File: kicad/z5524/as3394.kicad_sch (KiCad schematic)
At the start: 35 parts, among them U11 DG442xY, U14 TL074, U15 AS3394

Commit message: dist ref cap to two 1u instead of single; some more silkscreen cleanup
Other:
- moved on the sheet: C44, C45, C46, C50, C53, C55, C60, C62, C64, C66, D3, D4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

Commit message: v0.3 Release
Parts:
- U11: value DG442xY -> DG442DY-T1-E3; LCSC C144269 -> C2673321
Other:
- note added: "Saw: +/-2.84V"
- note added: "TODO: use a 68k Basic part and re-eval VCO Output levels: expected levels differ from observed levels at 63x gain Waveshape Expected Observed Saw +/- 2.84V +/- 1.64V Tri +/- 3.15V -1.8 : +1.32V Saw+Tri -5.67 +2.84 -2.8 : +1.76V Pulse +/- 1.9V"
- note removed: "Saw: +/-2.8V TODO: measure observed"
- note removed: "VCO Output levels: expected levels differ from observed levels at 63x gain Waveshape Expected Observed Saw +/- 2.84V +/- 1.64V Tri +/- 3.15V -1.8 : +1.32V Saw+Tri -5.67 +2.84 -2.8 : +1.76V Pulse +/- 1.9V"
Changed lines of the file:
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@@
   (title_block
     (title "Zoxnoxious Z5524 (SSI2130/AS3394)")
-    (date "2023-12-06")
+    (date "2023-12-12")
     (rev "0.3")
     (company "Zoxnoxious Engineering")
@@
     (effects (font (size 1.27 1.27)) (justify left bottom))
   )
-  (text "Saw: +/-2.8V\nTODO: measure observed" (at 231.775 113.03 0)
+  (text "Saw: +/-2.84V" (at 231.775 113.03 0)
     (effects (font (size 1.27 1.27)) (justify left bottom))
   )
-  (text "VCO Output levels: expected levels\ndiffer from observed levels at 63x gain\nWaveshape	Expected			Observed\nSaw			+/- 2.84V		+/- 1.64V\nTri			+/- 3.15V		-1.8 : +1.32V\nSaw+Tri		-5.67 +2.84		-2.8 : +1.76V\nPulse		+/- 1.9V			"
+  (text "TODO: use a 68k Basic part and re-eval\nVCO Output levels: expected levels\ndiffer from observed levels at 63x gain\nWaveshape	Expected			Observed\nSaw			+/- 2.84V		+/- 1.64V\nTri			+/- 3.15V		-1.8 : +1.32V\nSaw+Tri		-5.67 +2.84		-2.8 : +1.76V\nPulse		+/- 1.9V			"
     (at 201.295 94.615 0)
     (effects (font (size 1.27 1.27)) (justify left bottom))
@@
       (effects (font (size 1.27 1.27)))
     )
-    (property "Value" "DG442xY" (at 331.47 67.4171 0)
+    (property "Value" "DG442DY-T1-E3" (at 331.47 67.4171 0)
       (effects (font (size 1.27 1.27)))
     )
@@
       (effects (font (size 1.27 1.27)) hide)
     )
-    (property "LCSC" "C144269" (at 331.47 71.12 0)
-      (effects (font (size 1.27 1.27)) hide)
-    )
+    (property "LCSC" "C2673321" (at 331.47 71.12 0)
+      (effects (font (size 1.27 1.27)) hide)
+    )

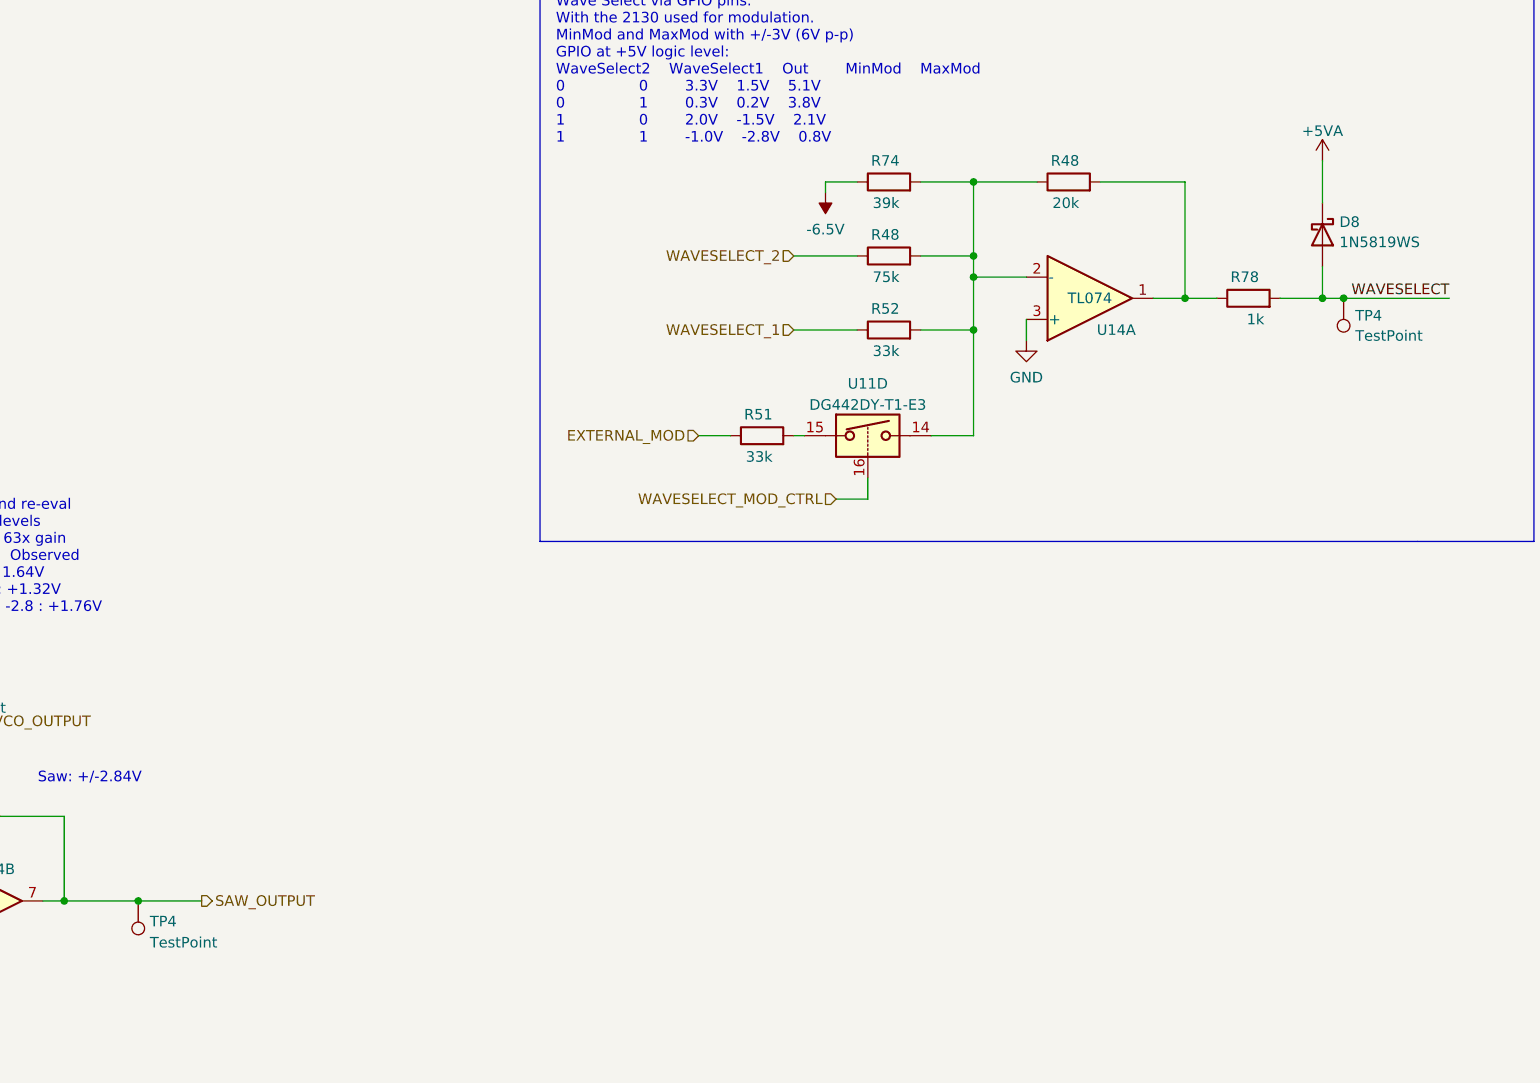
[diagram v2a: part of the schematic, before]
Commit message: updated routing and prep for z5524 revision rev.  Power routing going from polygons to direct
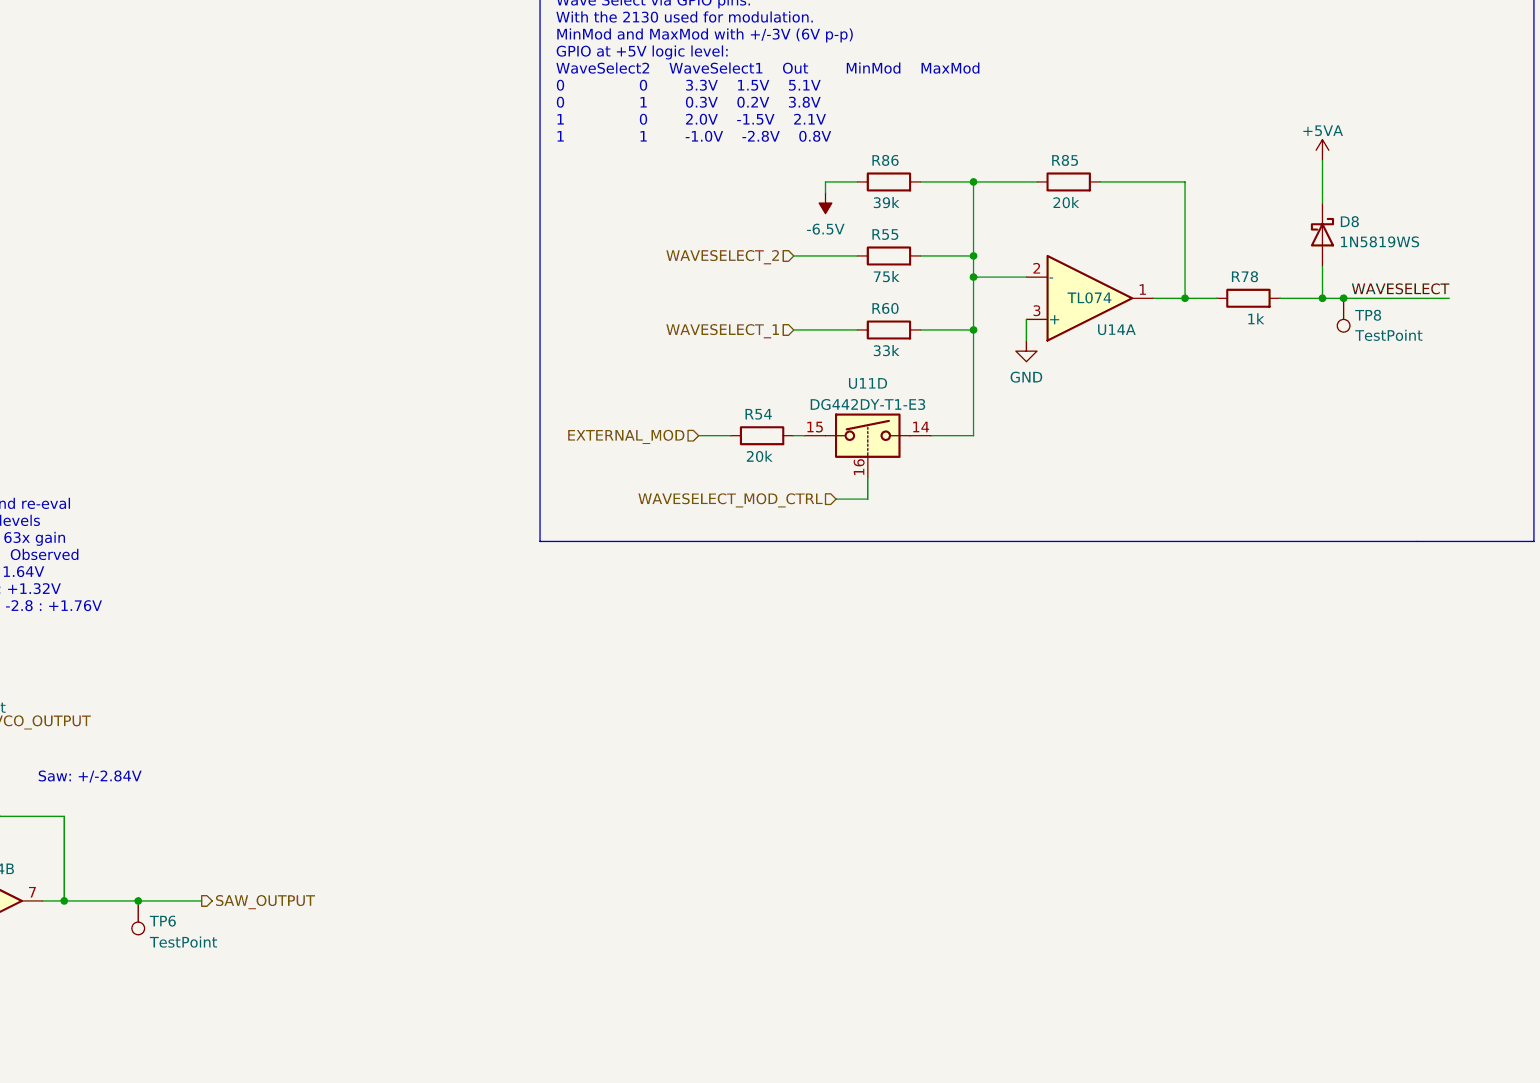
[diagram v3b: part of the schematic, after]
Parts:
- R54: renamed from R51; value 33k -> 20k; LCSC C4216 -> (none)
- renumbered R48 to R55, R52 to R60, R48 to R85, R74 to R86, TP4 to TP6, TP4 to TP8
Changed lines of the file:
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@@
   (symbol (lib_id "Device:R") (at 355.6 40.64 90) (unit 1)
     (in_bom yes) (on_board yes) (dnp no)
-    (property "Reference" "R48" (at 356.87 38.1 90)
+    (property "Reference" "R85" (at 356.87 38.1 90)
       (effects (font (size 1.27 1.27)) (justify left))
     )
@@
     (instances
       (project "z5524"
-        (path "/7079bdb0-a00e-4bac-b257-cbcf2c91bbd6"
-          (reference "R48") (unit 1)
-        )
         (path "/7079bdb0-a00e-4bac-b257-cbcf2c91bbd6/998834c5-8208-4d7e-a084-854ca45521ff"
           (reference "R85") (unit 1)
@@
   (symbol (lib_id "Device:R") (at 334.01 49.53 90) (unit 1)
     (in_bom yes) (on_board yes) (dnp no)
-    (property "Reference" "R48" (at 335.28 46.99 90)
+    (property "Reference" "R55" (at 335.28 46.99 90)
       (effects (font (size 1.27 1.27)) (justify left))
     )
@@
     (instances
       (project "z5524"
-        (path "/7079bdb0-a00e-4bac-b257-cbcf2c91bbd6"
-          (reference "R48") (unit 1)
-        )
         (path "/7079bdb0-a00e-4bac-b257-cbcf2c91bbd6/998834c5-8208-4d7e-a084-854ca45521ff"
           (reference "R55") (unit 1)
@@
   (symbol (lib_id "Device:R") (at 334.01 40.64 90) (unit 1)
     (in_bom yes) (on_board yes) (dnp no)
-    (property "Reference" "R74" (at 335.28 38.1 90)
+    (property "Reference" "R86" (at 335.28 38.1 90)
       (effects (font (size 1.27 1.27)) (justify left))
     )
@@
     (instances
       (project "z5524"
-        (path "/7079bdb0-a00e-4bac-b257-cbcf2c91bbd6"
+        (path "/7079bdb0-a00e-4bac-b257-cbcf2c91bbd6/998834c5-8208-4d7e-a084-854ca45521ff"
+          (reference "R86") (unit 1)
+        )
+      )
+    )
+  )
+  (symbol (lib_id "Device:R") (at 208.28 124.46 90) (unit 1)
+    (in_bom yes) (on_board yes) (dnp no)
+    (property "Reference" "R80" (at 209.55 121.92 90)
+      (effects (font (size 1.27 1.27)) (justify left))
+    )
+    (property "Value" "1k" (at 210.185 127 90)
+      (effects (font (size 1.27 1.27)) (justify left))
+    )
+    (property "Footprint" "Resistor_SMD:R_0603_1608Metric" (at 208.28 126.238 90)
+      (effects (font (size 1.27 1.27)) hide)
+    )
+    (property "Datasheet" "~" (at 208.28 124.46 0)
+      (effects (font (size 1.27 1.27)) hide)
+    )
+    (property "LCSC" "C21190" (at 208.28 124.46 0)
+      (effects (font (size 1.27 1.27)) hide)
+    )
+    (pin "1")
+    (pin "2")
+    (instances
+      (project "z5524"
+        (path "/7079bdb0-a00e-4bac-b257-cbcf2c91bbd6/998834c5-8208-4d7e-a084-854ca45521ff"
+          (reference "R80") (unit 1)
+        )
+      )
+    )
+  )
+  (symbol (lib_id "Device:R") (at 59.69 34.29 90) (unit 1)
+    (in_bom yes) (on_board yes) (dnp no)
+    (property "Reference" "R74" (at 58.42 39.37 0)
+      (effects (font (size 1.27 1.27)) (justify left))
+    )
+    (property "Value" "75k" (at 60.96 40.64 0)
+      (effects (font (size 1.27 1.27)) (justify left))
+    )
+    (property "Footprint" "Resistor_SMD:R_0603_1608Metric" (at 59.69 36.068 90)
+      (effects (font (size 1.27 1.27)) hide)
+    )
+    (property "Datasheet" "~" (at 59.69 34.29 0)
+      (effects (font (size 1.27 1.27)) hide)
+    )
+    (property "LCSC" "C23242" (at 59.69 34.29 0)
+      (effects (font (size 1.27 1.27)) hide)
+    )
+    (pin "1")
+    (pin "2")
+    (instances
+      (project "z5524"
+        (path "/7079bdb0-a00e-4bac-b257-cbcf2c91bbd6/998834c5-8208-4d7e-a084-854ca45521ff"
           (reference "R74") (unit 1)
         )
-        (path "/7079bdb0-a00e-4bac-b257-cbcf2c91bbd6/998834c5-8208-4d7e-a084-854ca45521ff"
-          (reference "R86") (unit 1)
-        )
-      )
-    )
-  )
-  (symbol (lib_id "Device:R") (at 208.28 124.46 90) (unit 1)
-    (in_bom yes) (on_board yes) (dnp no)
-    (property "Reference" "R80" (at 209.55 121.92 90)
-      (effects (font (size 1.27 1.27)) (justify left))
-    )
-    (property "Value" "1k" (at 210.185 127 90)
-      (effects (font (size 1.27 1.27)) (justify left))
-    )
-    (property "Footprint" "Resistor_SMD:R_0603_1608Metric" (at 208.28 126.238 90)
-      (effects (font (size 1.27 1.27)) hide)
-    )
-    (property "Datasheet" "~" (at 208.28 124.46 0)
-      (effects (font (size 1.27 1.27)) hide)
-    )
-    (property "LCSC" "C21190" (at 208.28 124.46 0)
-      (effects (font (size 1.27 1.27)) hide)
-    )
-    (pin "1")
-    (pin "2")
-    (instances
-      (project "z5524"
-        (path "/7079bdb0-a00e-4bac-b257-cbcf2c91bbd6/998834c5-8208-4d7e-a084-854ca45521ff"
-          (reference "R80") (unit 1)
-        )
-      )
-    )
-  )
-  (symbol (lib_id "Device:R") (at 59.69 34.29 90) (unit 1)
-    (in_bom yes) (on_board yes) (dnp no)
-    (property "Reference" "R74" (at 58.42 39.37 0)
-      (effects (font (size 1.27 1.27)) (justify left))
-    )
-    (property "Value" "75k" (at 60.96 40.64 0)
-      (effects (font (size 1.27 1.27)) (justify left))
-    )
-    (property "Footprint" "Resistor_SMD:R_0603_1608Metric" (at 59.69 36.068 90)
-      (effects (font (size 1.27 1.27)) hide)
-    )
-    (property "Datasheet" "~" (at 59.69 34.29 0)
-      (effects (font (size 1.27 1.27)) hide)
-    )
-    (property "LCSC" "C23242" (at 59.69 34.29 0)
-      (effects (font (size 1.27 1.27)) hide)
-    )
-    (pin "1")
-    (pin "2")
-    (instances
-      (project "z5524"
-        (path "/7079bdb0-a00e-4bac-b257-cbcf2c91bbd6/998834c5-8208-4d7e-a084-854ca45521ff"
-          (reference "R74") (unit 1)
-        )
       )
     )
@@
   (symbol (lib_id "Device:R") (at 318.77 71.12 90) (unit 1)
     (in_bom yes) (on_board yes) (dnp no)
-    (property "Reference" "R51" (at 320.04 68.58 90)
-      (effects (font (size 1.27 1.27)) (justify left))
-    )
-    (property "Value" "33k" (at 320.04 73.66 90)
+    (property "Reference" "R54" (at 320.04 68.58 90)
+      (effects (font (size 1.27 1.27)) (justify left))
+    )
+    (property "Value" "20k" (at 320.04 73.66 90)
       (effects (font (size 1.27 1.27)) (justify left))
     )
@@
       (effects (font (size 1.27 1.27)) hide)
     )
-    (property "LCSC" "C4216" (at 318.77 71.12 0)
-      (effects (font (size 1.27 1.27)) hide)
-    )
-    (pin "1")
-    (pin "2")
-    (instances
-      (project "z5524"
-        (path "/7079bdb0-a00e-4bac-b257-cbcf2c91bbd6"
-          (reference "R51") (unit 1)
-        )
+    (property "LCSC" "" (at 318.77 71.12 0)
+      (effects (font (size 1.27 1.27)) hide)
+    )
+    (pin "1")
+    (pin "2")
+    (instances
+      (project "z5524"
         (path "/7079bdb0-a00e-4bac-b257-cbcf2c91bbd6/998834c5-8208-4d7e-a084-854ca45521ff"
           (reference "R54") (unit 1)
@@
   (symbol (lib_id "Connector:TestPoint") (at 388.62 54.61 180) (unit 1)
     (in_bom yes) (on_board yes) (dnp no) (fields_autoplaced)
-    (property "Reference" "TP4" (at 390.017 56.6999 0)
+    (property "Reference" "TP8" (at 390.017 56.6999 0)
       (effects (font (size 1.27 1.27)) (justify right))
     )
@@
     (instances
       (project "z5524"
-        (path "/7079bdb0-a00e-4bac-b257-cbcf2c91bbd6"
-          (reference "TP4") (unit 1)
-        )
         (path "/7079bdb0-a00e-4bac-b257-cbcf2c91bbd6/998834c5-8208-4d7e-a084-854ca45521ff"
           (reference "TP8") (unit 1)
@@
     (instances
       (project "z5524"
-        (path "/7079bdb0-a00e-4bac-b257-cbcf2c91bbd6"
-          (reference "#PWR018") (unit 1)
-        )
         (path "/7079bdb0-a00e-4bac-b257-cbcf2c91bbd6/998834c5-8208-4d7e-a084-854ca45521ff"
           (reference "#PWR018") (unit 1)
@@
   (symbol (lib_id "Device:R") (at 334.01 58.42 90) (unit 1)
     (in_bom yes) (on_board yes) (dnp no)
-    (property "Reference" "R52" (at 335.28 55.88 90)
+    (property "Reference" "R60" (at 335.28 55.88 90)
       (effects (font (size 1.27 1.27)) (justify left))
     )
@@
     (instances
       (project "z5524"
-        (path "/7079bdb0-a00e-4bac-b257-cbcf2c91bbd6"
-          (reference "R52") (unit 1)
-        )
         (path "/7079bdb0-a00e-4bac-b257-cbcf2c91bbd6/998834c5-8208-4d7e-a084-854ca45521ff"
           (reference "R60") (unit 1)
@@
   (symbol (lib_id "Connector:TestPoint") (at 243.84 127 180) (unit 1)
     (in_bom yes) (on_board yes) (dnp no) (fields_autoplaced)
-    (property "Reference" "TP4" (at 245.237 129.4673 0)
+    (property "Reference" "TP6" (at 245.237 129.4673 0)
       (effects (font (size 1.27 1.27)) (justify right))
     )
@@
     (instances
       (project "z5524"
-        (path "/7079bdb0-a00e-4bac-b257-cbcf2c91bbd6"
-          (reference "TP4") (unit 1)
-        )
         (path "/7079bdb0-a00e-4bac-b257-cbcf2c91bbd6/998834c5-8208-4d7e-a084-854ca45521ff"
           (reference "TP6") (unit 1)
@@
     (instances
       (project "z5524"
-        (path "/7079bdb0-a00e-4bac-b257-cbcf2c91bbd6"
+        (path "/7079bdb0-a00e-4bac-b257-cbcf2c91bbd6/998834c5-8208-4d7e-a084-854ca45521ff"
           (reference "U11") (unit 4)
-        )
-        (path "/7079bdb0-a00e-4bac-b257-cbcf2c91bbd6/998834c5-8208-4d7e-a084-854ca45521ff"
-          (reference "U11") (unit 4)

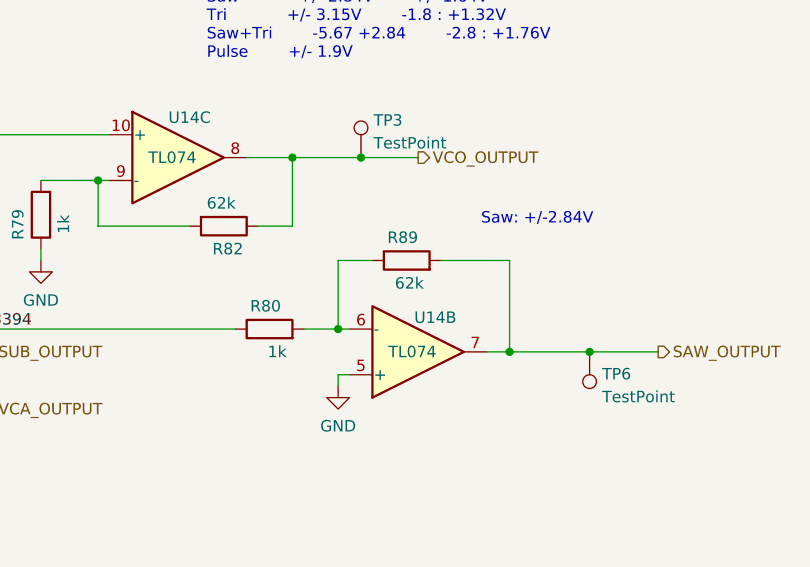
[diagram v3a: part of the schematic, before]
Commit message: fix soft sync.  tweak routing
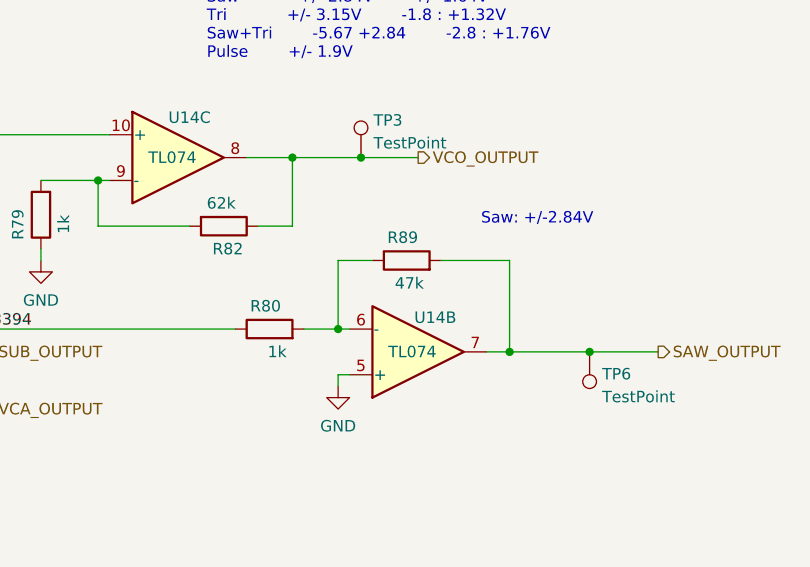
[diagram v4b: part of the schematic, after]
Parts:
- R89: value 62k -> 47k; LCSC C23221 -> C25819
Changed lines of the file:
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@@
       (effects (font (size 1.27 1.27)) (justify left))
     )
-    (property "Value" "62k" (at 225.425 119.38 90)
+    (property "Value" "47k" (at 225.425 119.38 90)
       (effects (font (size 1.27 1.27)) (justify left))
     )
@@
       (effects (font (size 1.27 1.27)) hide)
     )
-    (property "LCSC" "C23221" (at 223.52 116.84 90)
+    (property "LCSC" "C25819" (at 223.52 116.84 90)
       (effects (font (size 1.27 1.27)) hide)
     )
